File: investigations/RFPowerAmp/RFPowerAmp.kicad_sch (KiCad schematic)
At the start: 0 parts

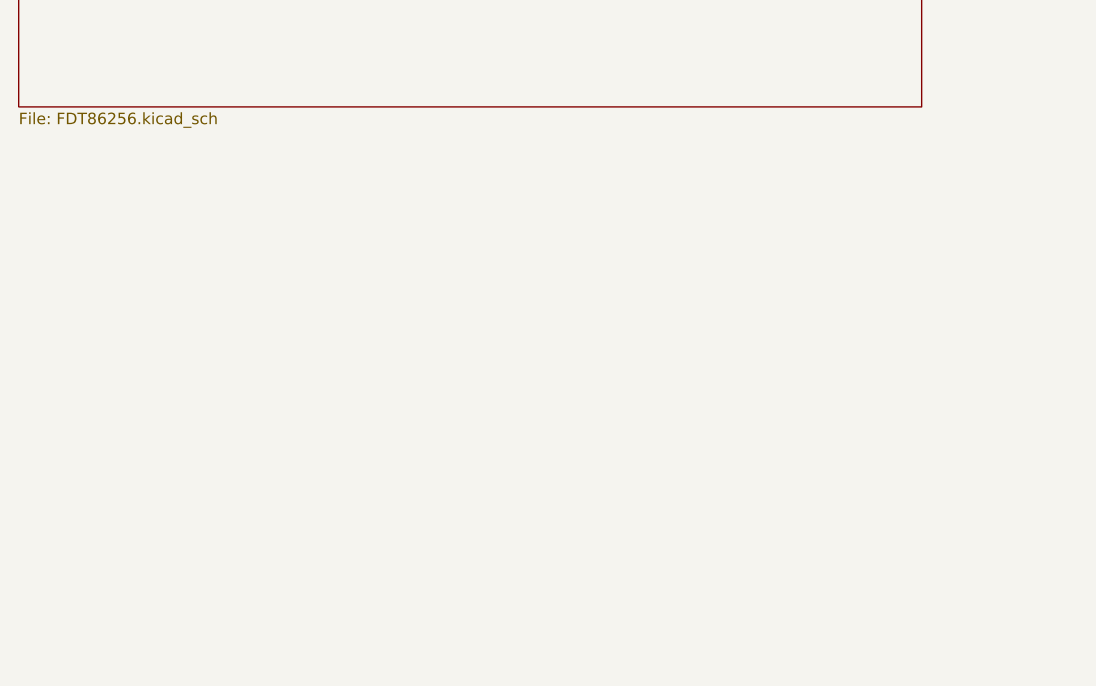
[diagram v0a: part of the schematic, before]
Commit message: Moving Pwr/tcxo to its own sheet
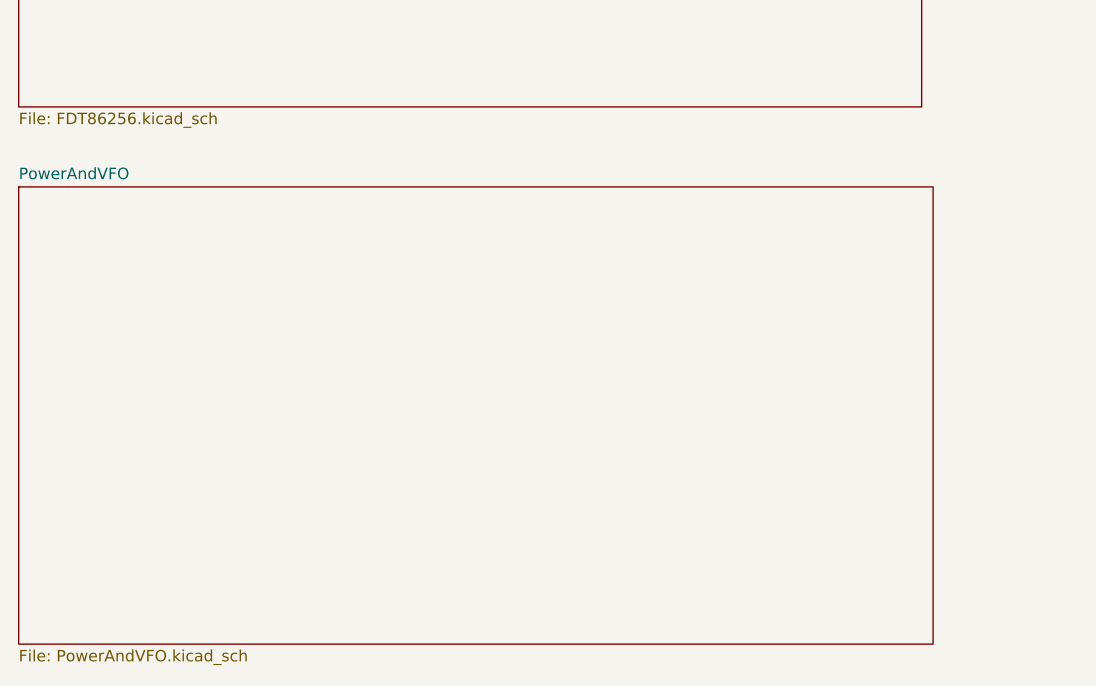
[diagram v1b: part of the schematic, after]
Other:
- added sheet PowerAndVFO (PowerAndVFO.kicad_sch)
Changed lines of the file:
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@@
 (kicad_sch (version 20230121) (generator eeschema)
   (paper "A4")
+  (sheet (at 20.32 139.7) (size 101.6 50.8) (fields_autoplaced)
+    (stroke (width 0.1524) (type solid))
+    (fill (color 0 0 0 0.0000))
+    (property "Sheetname" "PowerAndVFO" (at 20.32 138.9884 0)
+      (effects (font (size 1.27 1.27)) (justify left bottom))
+    )
+    (property "Sheetfile" "PowerAndVFO.kicad_sch" (at 20.32 191.0846 0)
+      (effects (font (size 1.27 1.27)) (justify left top))
+    )
+    (instances
+      (project "RFPowerAmp"
+        (path "/4eeb911c-75f4-4119-b54f-fc9266b9abf0" (page "6"))
+      )
+    )
+  )
   (sheet (at 172.72 82.55) (size 100.33 49.53) (fields_autoplaced)
     (stroke (width 0.1524) (type solid))

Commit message: simulations
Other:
- sheet FDT86256 renamed FDT86246
- removed sheet IRF510
- sheet FDT86246: file FDT86256.kicad_sch -> FDT86246.kicad_sch
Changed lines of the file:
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@@
     (stroke (width 0.1524) (type solid))
     (fill (color 0 0 0 0.0000))
-    (property "Sheetname" "FDT86256" (at 20.32 80.5684 0)
+    (property "Sheetname" "FDT86246" (at 20.32 80.5684 0) (show_name)
       (effects (font (size 1.27 1.27)) (justify left bottom))
     )
-    (property "Sheetfile" "FDT86256.kicad_sch" (at 20.32 131.3946 0)
+    (property "Sheetfile" "FDT86246.kicad_sch" (at 20.32 131.3946 0)
       (effects (font (size 1.27 1.27)) (justify left top))
     )
@@
       )
     )
-  )
-  (sheet (at 20.32 22.86) (size 100.33 48.26) (fields_autoplaced)
-    (stroke (width 0.1524) (type solid))
-    (fill (color 0 0 0 0.0000))
-    (property "Sheetname" "IRF510" (at 20.32 22.1484 0)
-      (effects (font (size 1.27 1.27)) (justify left bottom))
-    )
-    (property "Sheetfile" "IRF510.kicad_sch" (at 20.32 71.7046 0)
-      (effects (font (size 1.27 1.27)) (justify left top))
-    )
-    (instances
-      (project "RFPowerAmp"
-        (path "/4eeb911c-75f4-4119-b54f-fc9266b9abf0" (page "2"))
-      )
-    )
